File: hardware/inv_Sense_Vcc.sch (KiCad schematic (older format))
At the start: 7 parts, among them U1 ATtiny44-20SSU

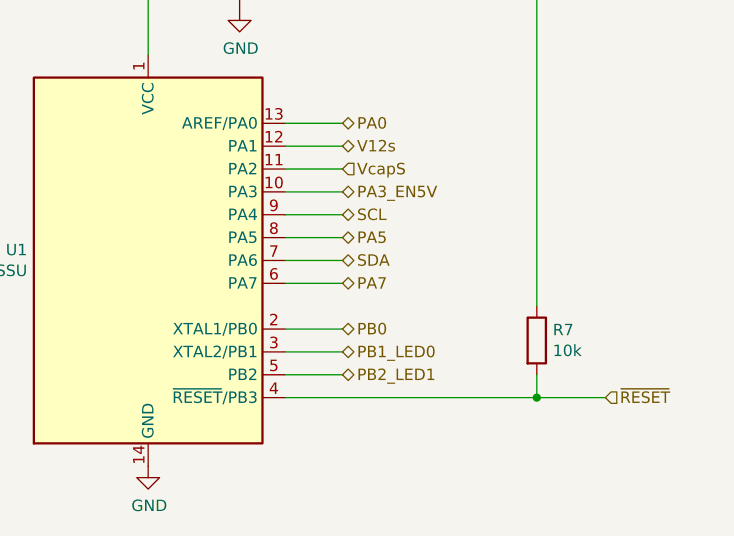
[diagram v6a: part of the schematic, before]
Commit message: Fix component values etc
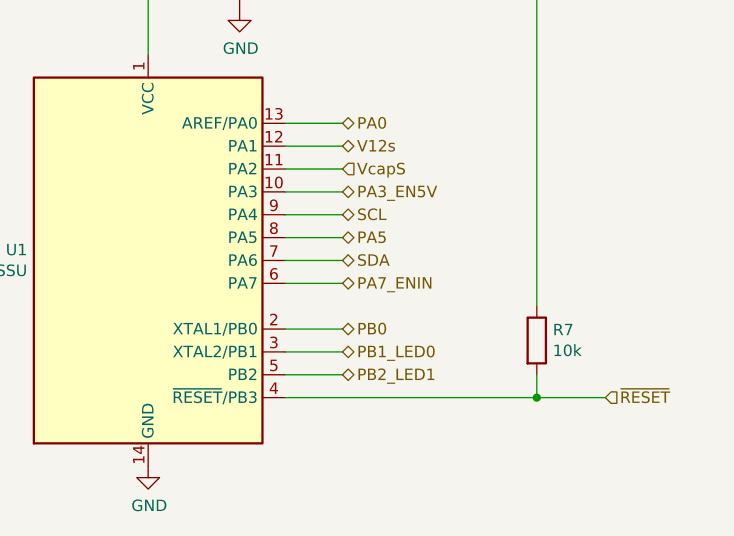
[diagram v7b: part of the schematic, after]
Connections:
- net PA7 renamed PA7_ENIN
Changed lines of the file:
@@
 PA5
 Text HLabel 4650 4600 2    50   BiDi ~ 0
-PA7
+PA7_ENIN
 Text HLabel 4650 4200 2    50   BiDi ~ 0
 PA3_EN5V
